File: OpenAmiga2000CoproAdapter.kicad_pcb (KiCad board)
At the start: 2 copper layers, 188.6 x 114.2 mm, 76 parts, among them CN1 A2000_COPRO_SLOT, P1 CONN_2, P10 CONN_1, P11 CONN_1, P12 CONN_1, P13 CONN_1, P14 CONN_1, P15 CONN_1, P2 CONN_2, P3 CONN_2, P4 CONN_2, P5 CONN_1, P6 CONN_1, P7 CONN_1, P8 CONN_1, P9 CONN_1, P99 OSHW_LOGO, U1 68000D, U10 Spare, U11 74HCT00, U12 74HCT27, U13 74HCT74, U14 74F86, U15 74F74, U16 74HCT04, U17 74HCT112, U18 74F157, U19 74F157, U2 AS6C4008-55PCN, U3 AS6C4008-55PCN, U4 AS6C4008-55PCN, U5 AS6C4008-55PCN, U6 74HCT00, U7 74HCT32, U8 74HCT32, U9 74LS05

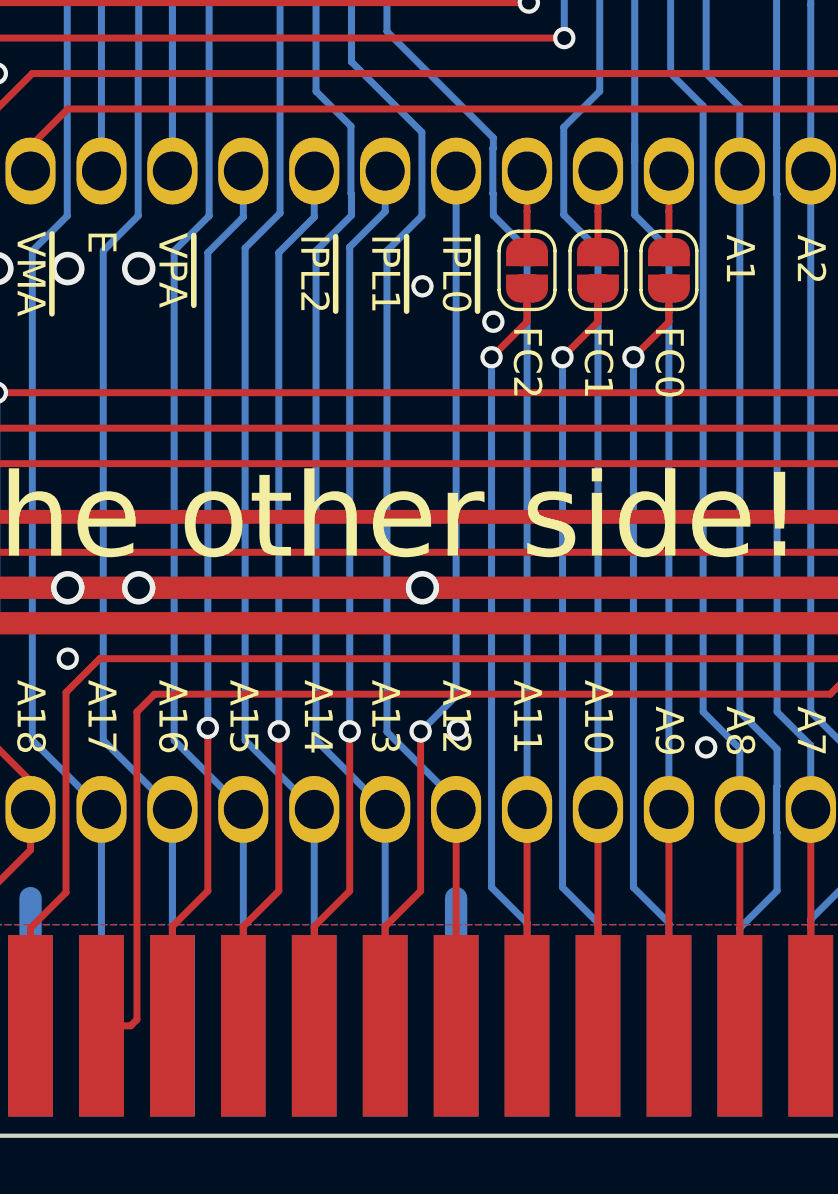
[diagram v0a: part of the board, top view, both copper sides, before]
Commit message: fix unconnected ground
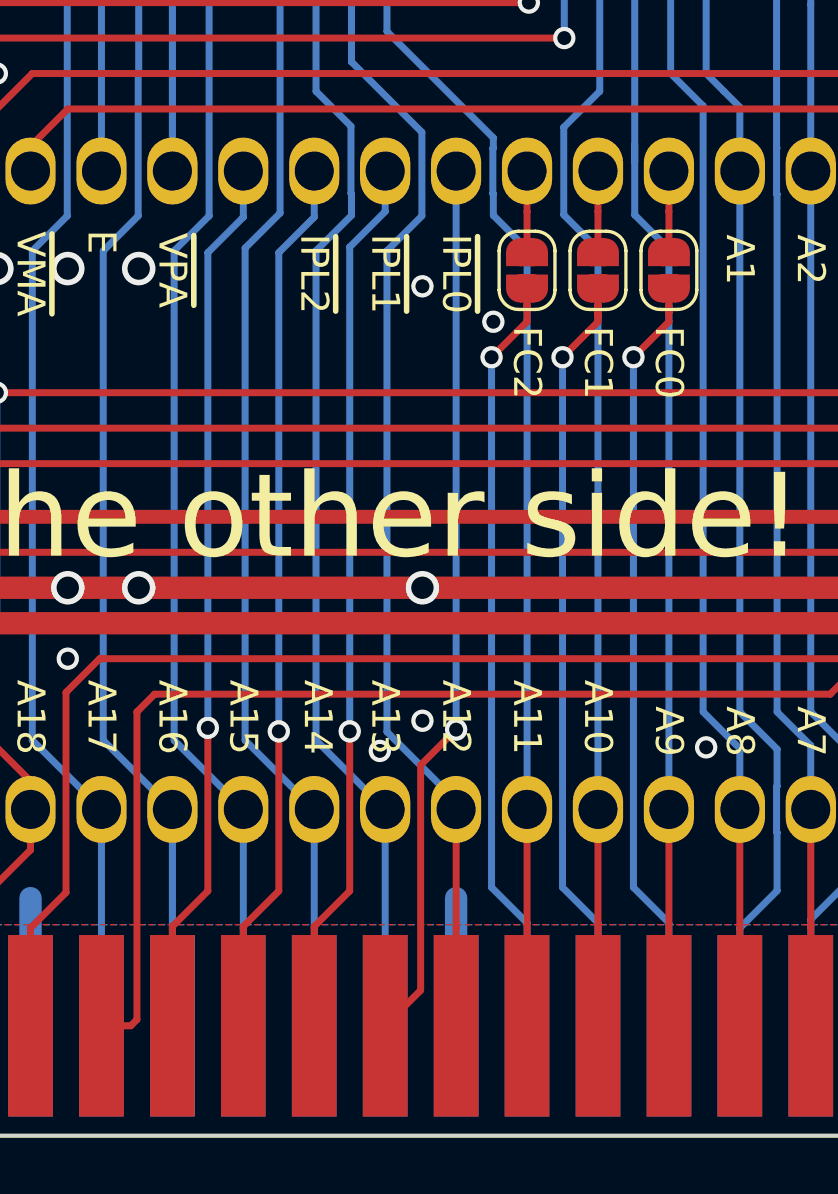
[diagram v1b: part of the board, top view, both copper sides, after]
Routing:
- net GND: vias 188 -> 189
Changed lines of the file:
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@@
     (thickness 1.6)
     (drawings 104)
-    (tracks 2301)
+    (tracks 2302)
     (zones 0)
     (modules 76)
@@
   (module OpenAmiga2000CoproAdapter:A2000_COPRO_SLOT (layer B.Cu)
     (at 179.578 147.7645 180)
-    (fp_text reference CN1 (at 33.02 -0.5) (layer B.SilkS) hide
+    (fp_text reference CN1 (at 33.02 -0.5 180) (layer B.SilkS) hide
       (effects (font (size 1 1) (thickness 0.15)) (justify mirror))
     )
-    (fp_text value A2000_COPRO_SLOT (at 33.02 0.5) (layer B.Fab)
+    (fp_text value A2000_COPRO_SLOT (at 33.02 0.5 180) (layer B.Fab)
       (effects (font (size 1 1) (thickness 0.15)) (justify mirror))
     )
@@
     (fp_line (start 89.027 1.143) (end -22.987 1.143) (layer B.CrtYd) (width 0.15))
     (fp_line (start -22.987 1.143) (end -22.987 8.382) (layer B.CrtYd) (width 0.15))
-    (fp_line (start -22.987 8.382) (end -25.4 8.382) (layer B.CrtYd) (width 0.15))
-    (fp_line (start 89.027 8.382) (end 91.567 8.382) (layer B.CrtYd) (width 0.15))
-    (fp_text user 86 (at 86.36 9.652) (layer F.SilkS)
+    (fp_text user 86 (at 86.36 9.652 180) (layer F.SilkS)
       (effects (font (size 1 1) (thickness 0.2)))
     )
-    (fp_text user 85 (at 86.36 9.652) (layer B.SilkS)
+    (fp_text user 85 (at 86.36 9.652 180) (layer B.SilkS)
       (effects (font (size 1 1) (thickness 0.2)) (justify mirror))
     )
-    (fp_text user 2 (at -20.32 9.652) (layer F.SilkS)
+    (fp_text user 2 (at -20.32 9.652 180) (layer F.SilkS)
       (effects (font (size 1 1) (thickness 0.2)))
     )
-    (fp_text user 1 (at -20.32 9.652) (layer B.SilkS)
+    (fp_text user 1 (at -20.32 9.652 180) (layer B.SilkS)
       (effects (font (size 1 1) (thickness 0.2)) (justify mirror))
     )
@@
   (via (at 140.2715 129.54) (size 0.8) (drill 0.5) (layers F.Cu B.Cu) (net 1))
   (via (at 155.5115 117.475) (size 0.8) (drill 0.5) (layers F.Cu B.Cu) (net 1))
-  (via (at 154.2415 132.08) (size 0.8) (drill 0.5) (layers F.Cu B.Cu) (net 1))
   (via (at 152.9715 116.205) (size 0.8) (drill 0.5) (layers F.Cu B.Cu) (net 1))
+  (via (at 151.4475 132.842) (size 0.8) (drill 0.5) (layers F.Cu B.Cu) (net 1))
+  (via (at 152.9715 131.7625) (size 0.8) (drill 0.5) (layers F.Cu B.Cu) (net 1))
   (segment (start 126.238 108.6485) (end 126.3015 108.585) (width 0.8) (layer F.Cu) (net 2))
   (segment (start 126.238 112.0775) (end 126.238 108.6485) (width 0.8) (layer F.Cu) (net 2))
@@
   (segment (start 126.3015 66.04) (end 127.5715 64.77) (width 0.25) (layer F.Cu) (net 108))
   (segment (start 103.4415 64.77) (end 110.4265 64.77) (width 0.25) (layer F.Cu) (net 108))
-  (segment (start 154.178 130.8735) (end 152.908 132.1435) (width 0.25) (layer B.Cu) (net 109))
-  (segment (start 154.178 112.0775) (end 154.178 130.8735) (width 0.25) (layer B.Cu) (net 109))
-  (via (at 152.908 132.1435) (size 0.8) (drill 0.5) (layers F.Cu B.Cu) (net 109))
-  (segment (start 151.638 139.1285) (end 151.638 142.6845) (width 0.25) (layer F.Cu) (net 109))
-  (segment (start 152.908 137.8585) (end 151.638 139.1285) (width 0.25) (layer F.Cu) (net 109))
-  (segment (start 152.908 132.1435) (end 152.908 137.8585) (width 0.25) (layer F.Cu) (net 109))
+  (segment (start 154.178 112.0775) (end 154.178 132.079996) (width 0.25) (layer B.Cu) (net 109))
+  (via (at 154.178004 132.08) (size 0.8) (drill 0.5) (layers F.Cu B.Cu) (net 109))
+  (segment (start 152.908 141.4145) (end 152.908 133.350004) (width 0.25) (layer F.Cu) (net 109))
+  (segment (start 154.178 132.079996) (end 154.178004 132.08) (width 0.25) (layer B.Cu) (net 109))
+  (segment (start 151.638 142.6845) (end 152.908 141.4145) (width 0.25) (layer F.Cu) (net 109))
+  (segment (start 152.908 133.350004) (end 154.178004 132.08) (width 0.25) (layer F.Cu) (net 109))
   (segment (start 151.638 142.6845) (end 151.638 134.9375) (width 0.25) (layer B.Cu) (net 110) (status 30))
   (segment (start 162.986501 62.23) (end 164.4015 62.23) (width 0.25) (layer F.Cu) (net 110))

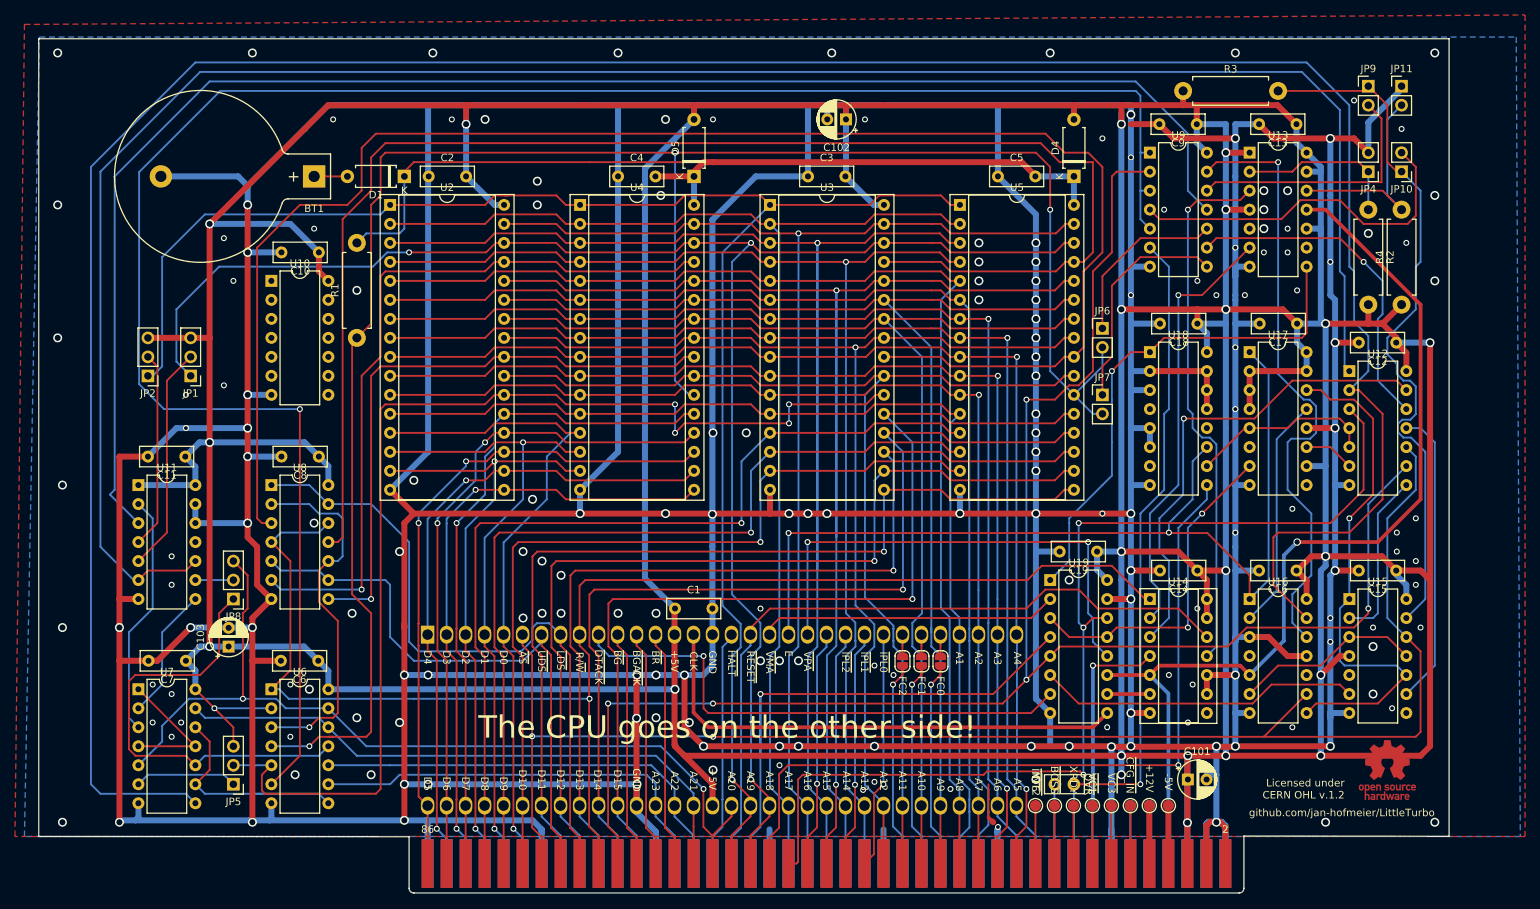
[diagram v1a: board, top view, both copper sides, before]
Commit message: silk screen
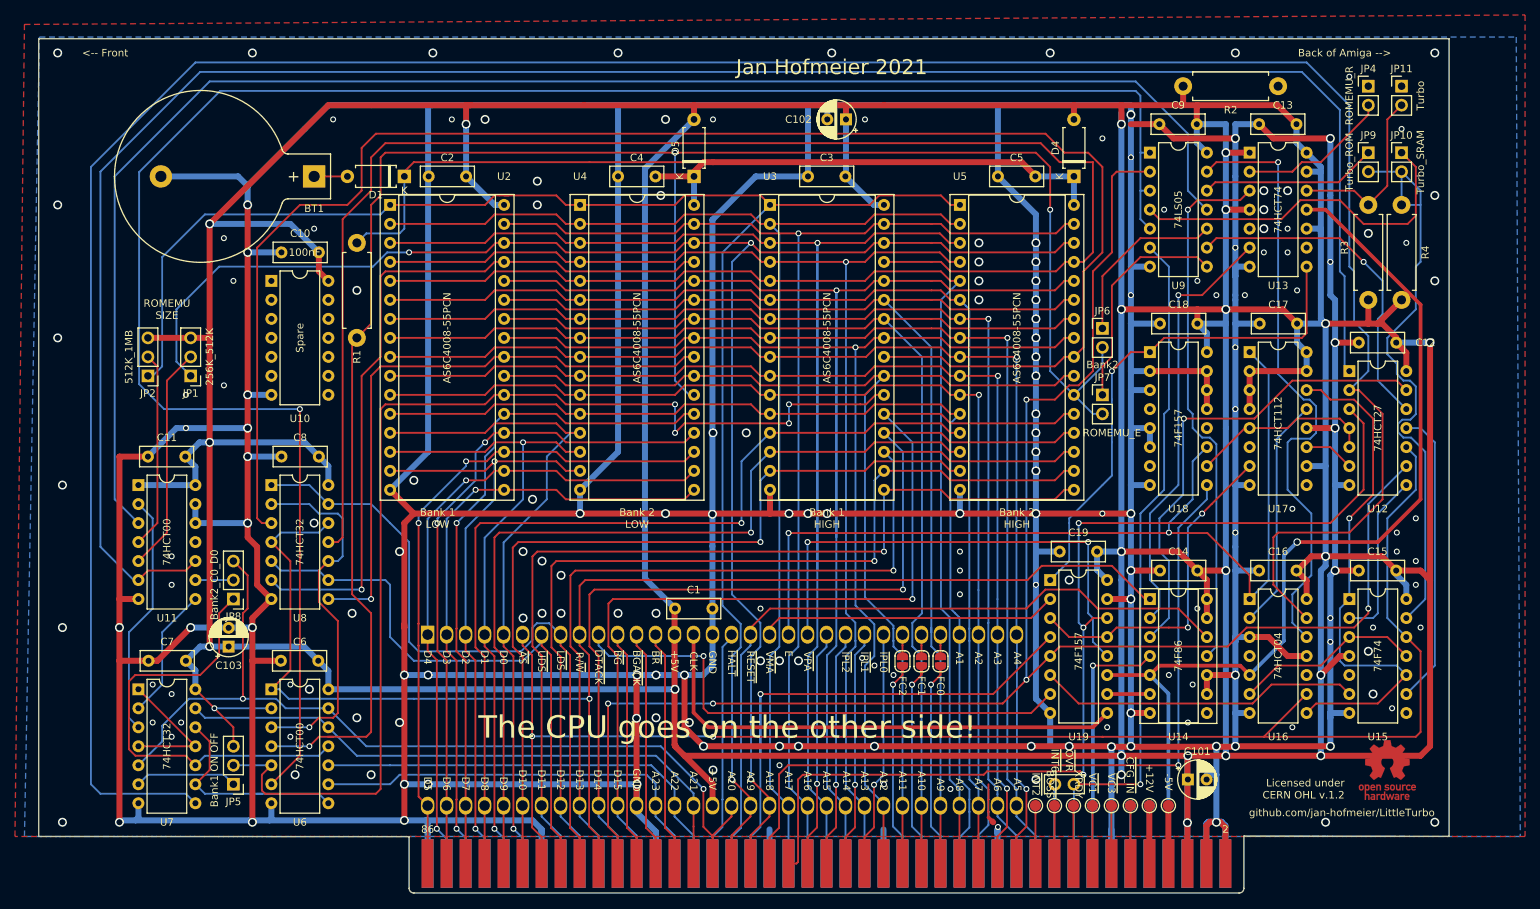
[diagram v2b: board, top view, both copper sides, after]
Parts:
- JP4: value ROMEMUW~R -> ROMEMU_R
- JP5: value Bank1_ON_OFF -> Bank1 ON OFF
- JP7: value ROMEMU -> ROMEMU_E
- moved R3 40.4 mm to (223.5, 67.3), turned to 90 degrees
- moved R2 29.8 mm to (194.2, 38.7), turned to 0 degrees
- moved JP4 11.4 mm to (219.0, 38.7), turned to 0 degrees
- moved JP9 8.89 mm to (219.0, 47.6)
- moved R4 4.49 mm to (219.0, 67.3)
- moved JP10 2.54 mm to (223.5, 47.6), turned to 0 degrees
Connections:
- JP10 pad 1: /Memory/~DTACK_FAST -> Net-(JP10-Pad1)
- JP10 pad 2: Net-(JP10-Pad2) -> /Memory/~DTACK_FAST
- JP4 pad 1: /Memory/ROM~R~W -> GND
- JP4 pad 2: GND -> /Memory/ROM~R~W
- JP9 pad 1: /Memory/~DTACK_FAST -> Net-(JP9-Pad1)
- JP9 pad 2: Net-(JP9-Pad2) -> /Memory/~DTACK_FAST
- U9 pad 12: Net-(JP9-Pad2) -> Net-(JP9-Pad1)
- U9 pad 4: Net-(JP10-Pad2) -> Net-(JP10-Pad1)
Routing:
- net Net-(JP10-Pad2): track 48.1 -> 0.00 mm
- net Net-(JP10-Pad1): track 0.00 -> 48.1 mm
- net Net-(JP9-Pad2): track 34.9 -> 0.00 mm
- net Net-(JP9-Pad1): track 0.00 -> 23.7 mm
- net GND: track 1503.7 -> 1487.5 mm, vias 189 -> 193
- net /Memory/~DTACK_FAST: track 95.4 -> 80.9 mm
- net Net-(JP11-Pad2): track 29.3 -> 24.2 mm
- net /Memory/ROM~R~W: track 22.6 -> 20.3 mm
- net +5V: track 1118.5 -> 1119.6 mm
- net /Memory/CSRAM2: track 211.1 -> 210.5 mm
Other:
- board text added: "<-- Back of Amiga"
- board text added: "<-- Front"
- board text added: "Back of Amiga -->"
- board text added: "Bank 1 HIGH"
- board text added: "Bank 1 LOW"
- board text added: "Bank 2 HIGH"
- board text added: "Bank 2 LOW"
- board text added: "Front -->"
- board text added: "Jan Hofmeier 2021"
- board text added: "MC68000"
- board text added: "ROMEMU SIZE"
- board text added: "Spare"

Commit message: rom mirror
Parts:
- JP4: value ROMEMU_R -> ROMEMUW~R
- JP5: value Bank1 ON OFF -> Bank1_ON_OFF
- JP7: value ROMEMU_E -> ROMEMU
- moved R2 12.7 mm to (206.9, 38.7), turned to 180 degrees
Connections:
- U11 pad 12: GND -> Net-(JP8-Pad1)
- U11 pad 13: GND -> Net-(JP1-Pad2)
- U12 pad 1: Net-(U11-Pad10) -> GND
- U14 pad 10: GND -> /a18
- U14 pad 8: Net-(U14-Pad8) -> /Memory/a18m
- U14 pad 9: GND -> Net-(U11-Pad11)
- U2 pad 30: /a18 -> /Memory/a18m
- U3 pad 30: /a18 -> /Memory/a18m
- U4 pad 30: /a18 -> /Memory/a18m
- U5 pad 30: /a18 -> /Memory/a18m
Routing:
- net Net-(U11-Pad10): track 274.6 -> 9.31 mm
- net /Memory/a18m: track 0.00 -> 195.7 mm, vias 0 -> 2
- net Net-(U11-Pad11): track 0.00 -> 159.6 mm, vias 0 -> 3
- net /a18: track 224.7 -> 198.6 mm, vias 3 -> 5
- net Net-(JP8-Pad1): track 59.6 -> 75.3 mm
- net GND: track 1487.5 -> 1472.6 mm, vias 193 -> 180
- net /Memory/ROM~R~W: track 20.3 -> 33.4 mm
- net /~vma: track 73.4 -> 83.0 mm
- net Net-(U13-Pad6): track 58.0 -> 63.5 mm
- net Net-(JP1-Pad2): track 30.2 -> 34.0 mm
- net /Memory/~CS2: track 263.2 -> 259.4 mm
- net /a12: track 151.0 -> 153.8 mm, vias 1 -> 0
- net /Memory/~LWE: track 194.5 -> 192.0 mm
- net Net-(U15-Pad6): track 43.2 -> 45.5 mm
- net Net-(JP7-Pad1): track 29.9 -> 27.8 mm
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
